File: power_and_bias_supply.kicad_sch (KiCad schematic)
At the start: 42 parts, among them Q501 2N7002, U501 MCP6L02x-xSN, U502 LM2733YMFX/NOPB, U503 TPS22944DCKR, X5 Conn_Coaxial

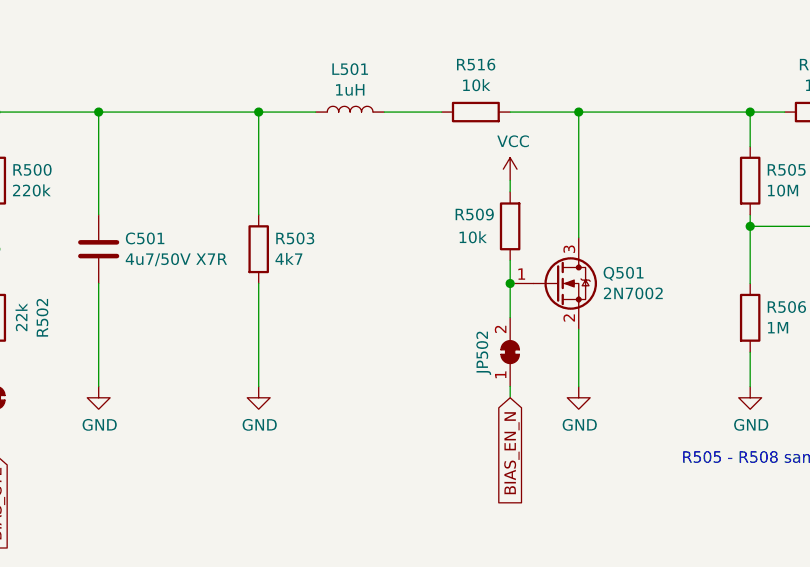
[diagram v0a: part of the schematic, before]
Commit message: Redesign of Board. Added optional Breakoutboars for ADC and DAC
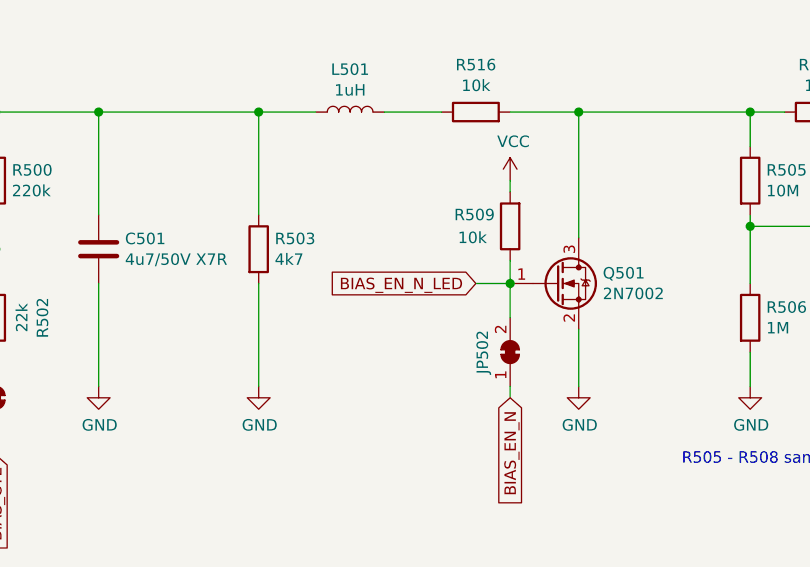
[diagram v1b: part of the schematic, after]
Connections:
- net BIAS_EN_N_LED: now reaches JP502.2 (B), Q501.1 (G), R509.1
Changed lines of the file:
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@@
+    (stroke (width 0) (type solid) (color 0 0 0 0))
+  )
+  (wire (pts (xy 143.51 91.44) (xy 147.32 91.44))
     (stroke (width 0) (type solid) (color 0 0 0 0))
   )
@@
     )
   )
+  (global_label "BIAS_EN_N_LED" (shape input) (at 143.51 91.44 180) (fields_autoplaced)
+    (effects (font (size 1.27 1.27)) (justify right))
+    (property "Intersheet References" "${INTERSHEET_REFS}" (id 0) (at 126.764 91.3606 0)
+      (effects (font (size 1.27 1.27)) (justify right) hide)
+    )
+  )

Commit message: some changes after first test of boards. Package of SN74LV221AD changed to SOIC-16.
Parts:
- C501, C550, C560: JLCplace (none) -> C29823; Supplier (none) -> LCSC
- C503, C504: JLCplace (none) -> C46653; Supplier (none) -> LCSC
- C505: JLCplace (none) -> C1716; Supplier (none) -> LCSC
- C520: JLCplace (none) -> C1710; Supplier (none) -> LCSC
- C553, C554, C569: JLCplace (none) -> C49678; Supplier (none) -> LCSC
- C568: JLCplace (none) -> C28323; Supplier (none) -> LCSC
- D500: Supplier (none) -> LCSC
- JP500, JP501, JP502, JP503, JP504, JP505, JP506, TP502, TP503, TP504, TP505: Supplier (none) -> --
- L500: Supplier LCSC -> Mouser
- Q501: JLCplace (none) -> C8545
- R500: JLCplace (none) -> C17556; Supplier (none) -> LCSC
- R501: JLCplace (none) -> C17455; Supplier (none) -> LCSC
- R502: JLCplace (none) -> C17560; Supplier (none) -> LCSC
- R503: JLCplace (none) -> C17673; Supplier (none) -> LCSC
- R504, R509, R512, R516: JLCplace (none) -> C17414; Supplier (none) -> LCSC
- R505, R507: JLCplace (none) -> C26108; Supplier (none) -> LCSC
- R506, R508: JLCplace (none) -> C17514; Supplier (none) -> LCSC
- U501: JLCBasicPart (none) -> Extended; JLCPartNr (none) -> C623781; JLCType (none) -> MCP6L02T-E/SN
- U503: JLCBasicPart (none) -> Extended; JLCPartNr (none) -> C200357; JLCType (none) -> TPS22944DCKR
- X5: JLCBasicPart (none) -> Extended; JLCPartNr (none) -> C88374; JLCType (none) -> U.FL-R-SMT-1(80); OriginalType (none) -> U.FL-R-SMT-1(80); Supplier (none) -> LCSC

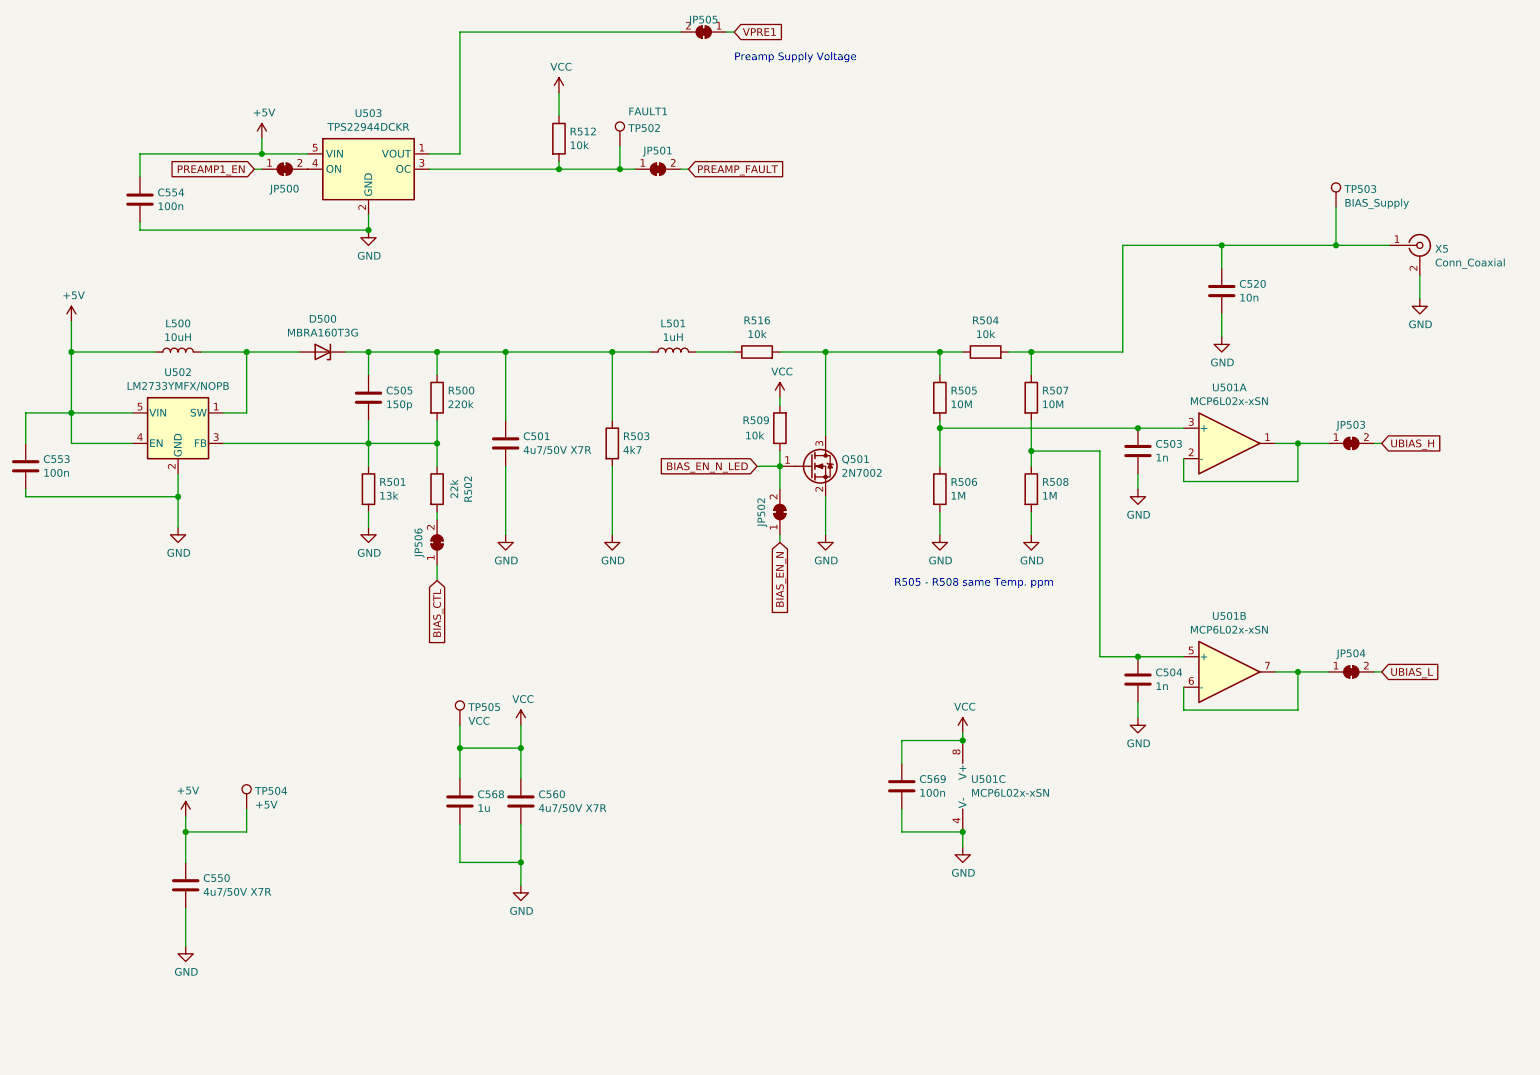
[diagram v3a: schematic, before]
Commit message: Refactored schematic to better show relationship in main schematic
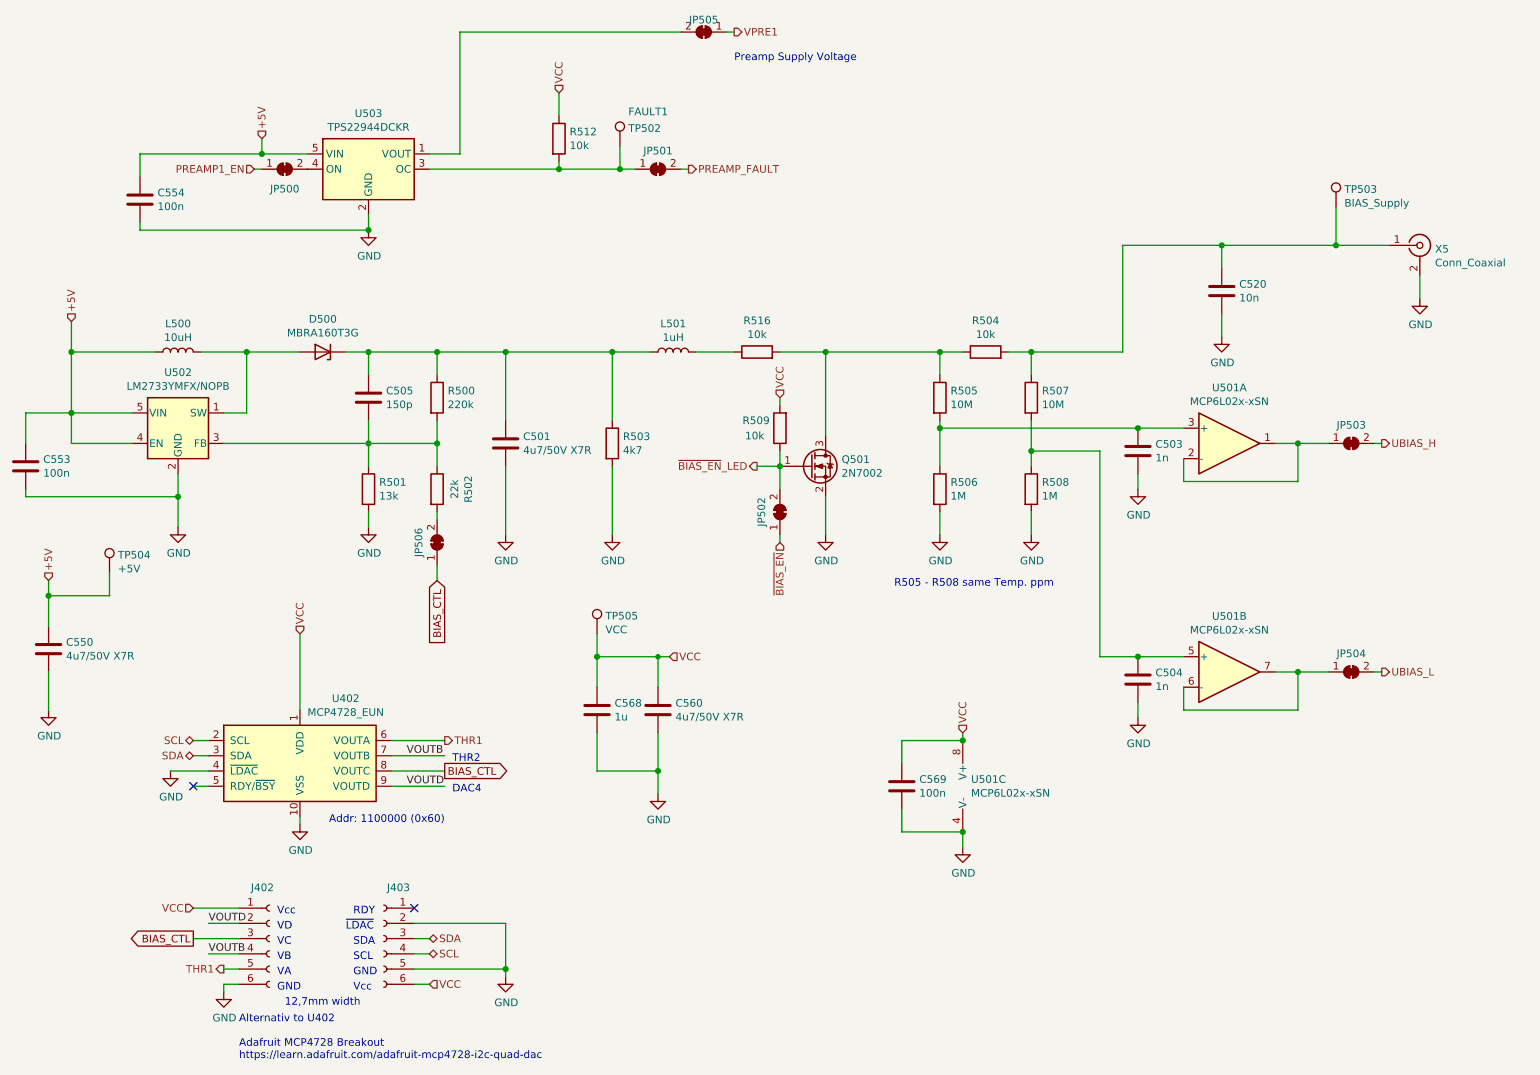
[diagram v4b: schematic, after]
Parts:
- added J402, J403: Conn_01x06_Female, Connector_PinSocket_2.54mm:PinSocket_1x06_P2.54mm_Vertical, symbol Connector:Conn_01x06_Female
- added U402: MCP4728_EUN, Package_SO:MSOP-10_3x3mm_P0.5mm, symbol Analog_DAC:MCP4728
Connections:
- net BIAS_CTL: now also J402.3 (Pin_3), U402.8 (VOUTC)
- net GND: now also J402.6 (Pin_6), J403.2 (Pin_2), J403.5 (Pin_5), U402.10 (VSS), U402.4 (~{LDAC})
- net VCC: now also J402.1 (Pin_1), J403.6 (Pin_6), U402.1 (VDD)
- net BIAS_EN_N renamed ~{BIAS_EN}
- net BIAS_EN_N_LED renamed ~{BIAS_EN}_LED
- new net SCL: J403.4 (Pin_4), U402.2 (SCL)
- new net SDA: J403.3 (Pin_3), U402.3 (SDA)
- new net THR1: J402.5 (Pin_5), U402.6 (VOUTA)
- new net VOUTB: J402.4 (Pin_4), U402.7 (VOUTB)
- new net VOUTD: J402.2 (Pin_2), U402.9 (VOUTD)
- no-connect marks 0 -> 2
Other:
- note added: "12,7mm width"
- note added: "Addr: 1100000 (0x60)"
- note added: "Alternativ to U402 Adafruit MCP4728 Breakout https://learn.adafruit.com/adafruit-mcp4728-i2c-quad-dac"
- note added: "DAC4"
- note added: "GND"
- note added: "RDY"
- note added: "SCL"
- note added: "SDA"
- note added: "THR2"
- note added: "VA"
- note added: "VB"
- note added: "VC"
- note added: "VD"
- note added: "Vcc"
- note added: "~{LDAC}"
- moved on the sheet: C550, C560, C568, TP504, TP505

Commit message: Cleaned up board, replaced GPIO footprint with unshrouded version
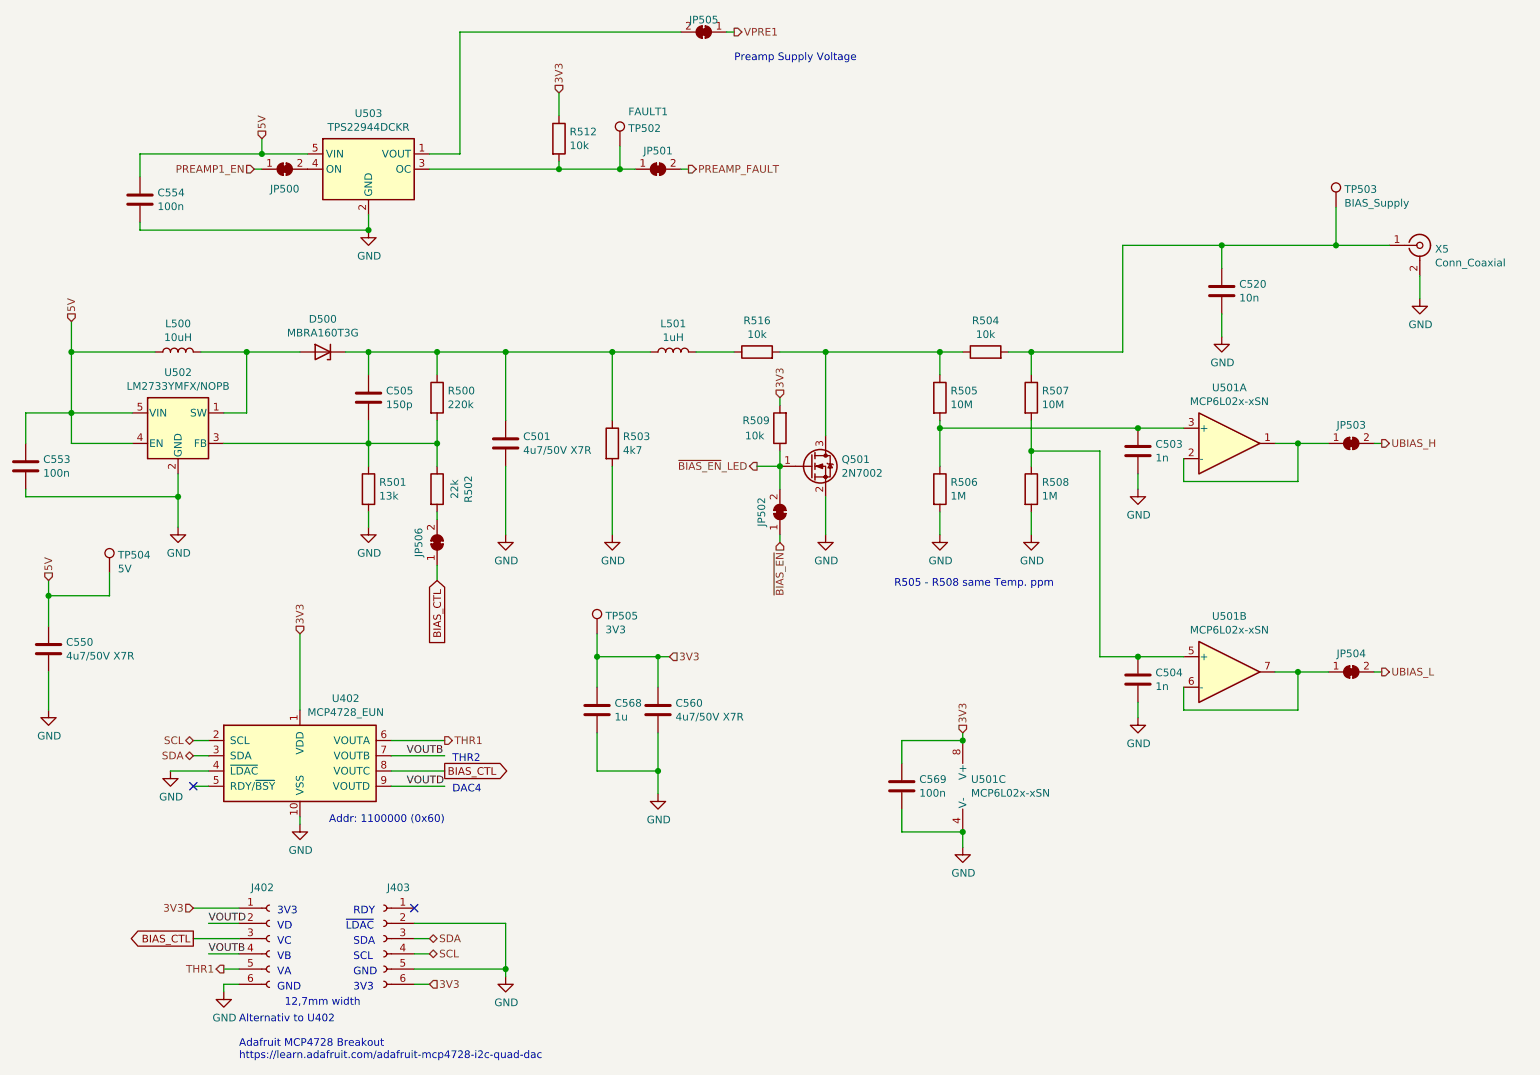
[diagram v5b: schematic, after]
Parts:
- TP504: value +5V -> 5V
- TP505: value VCC -> 3V3
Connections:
- net +5V renamed 5V
- net VCC renamed 3V3
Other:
- note added: "3V3"
- note removed: "Vcc"
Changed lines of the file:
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@@
     (effects (font (size 1.27 1.27)) (justify left bottom))
   )
-  (text "Vcc" (at 63.5 166.37 0)
+  (text "3V3" (at 63.5 166.37 0)
     (effects (font (size 1.27 1.27)) (justify left bottom))
   )
@@
     (effects (font (size 1.27 1.27)) (justify left bottom))
   )
-  (text "Vcc" (at 76.2 179.07 0)
+  (text "3V3" (at 76.2 179.07 0)
     (effects (font (size 1.27 1.27)) (justify left bottom))
   )
@@
     )
   )
-  (hierarchical_label "+5V" (shape input) (at 25.4 110.49 90)
+  (hierarchical_label "5V" (shape input) (at 25.4 110.49 90)
     (effects (font (size 1.27 1.27)) (justify left))
   )
-  (hierarchical_label "+5V" (shape input) (at 29.21 67.31 90)
+  (hierarchical_label "5V" (shape input) (at 29.21 67.31 90)
     (effects (font (size 1.27 1.27)) (justify left))
   )
@@
     (effects (font (size 1.27 1.27)) (justify right))
   )
-  (hierarchical_label "VCC" (shape input) (at 49.53 165.1 180)
+  (hierarchical_label "3V3" (shape input) (at 49.53 165.1 180)
     (effects (font (size 1.27 1.27)) (justify right))
   )
@@
     (effects (font (size 1.27 1.27)) (justify right))
   )
-  (hierarchical_label "+5V" (shape input) (at 60.96 36.83 90)
+  (hierarchical_label "5V" (shape input) (at 60.96 36.83 90)
     (effects (font (size 1.27 1.27)) (justify left))
   )
-  (hierarchical_label "VCC" (shape input) (at 67.31 119.38 90)
+  (hierarchical_label "3V3" (shape input) (at 67.31 119.38 90)
     (effects (font (size 1.27 1.27)) (justify left))
   )
@@
     (effects (font (size 1.27 1.27)) (justify left))
   )
-  (hierarchical_label "VCC" (shape input) (at 88.9 177.8 0)
+  (hierarchical_label "3V3" (shape input) (at 88.9 177.8 0)
     (effects (font (size 1.27 1.27)) (justify left))
   )
@@
     (effects (font (size 1.27 1.27)) (justify left))
   )
-  (hierarchical_label "VCC" (shape input) (at 110.49 29.21 90)
+  (hierarchical_label "3V3" (shape input) (at 110.49 29.21 90)
     (effects (font (size 1.27 1.27)) (justify left))
   )
-  (hierarchical_label "VCC" (shape input) (at 128.905 123.19 0)
+  (hierarchical_label "3V3" (shape input) (at 128.905 123.19 0)
     (effects (font (size 1.27 1.27)) (justify left))
   )
@@
     (effects (font (size 1.27 1.27)) (justify right))
   )
-  (hierarchical_label "VCC" (shape input) (at 147.32 80.01 90)
+  (hierarchical_label "3V3" (shape input) (at 147.32 80.01 90)
     (effects (font (size 1.27 1.27)) (justify left))
   )
@@
     (effects (font (size 1.27 1.27)) (justify right))
   )
-  (hierarchical_label "VCC" (shape input) (at 177.8 135.89 90)
+  (hierarchical_label "3V3" (shape input) (at 177.8 135.89 90)
     (effects (font (size 1.27 1.27)) (justify left))
   )
@@
       (effects (font (size 1.27 1.27)) (justify left))
     )
-    (property "Value" "+5V" (id 1) (at 36.9571 108.5278 0)
+    (property "Value" "5V" (id 1) (at 36.9571 108.5278 0)
       (effects (font (size 1.27 1.27)) (justify left))
     )
@@
       (effects (font (size 1.27 1.27)) (justify left))
     )
-    (property "Value" "VCC" (id 1) (at 118.2371 118.6878 0)
+    (property "Value" "3V3" (id 1) (at 118.2371 118.6878 0)
       (effects (font (size 1.27 1.27)) (justify left))
     )

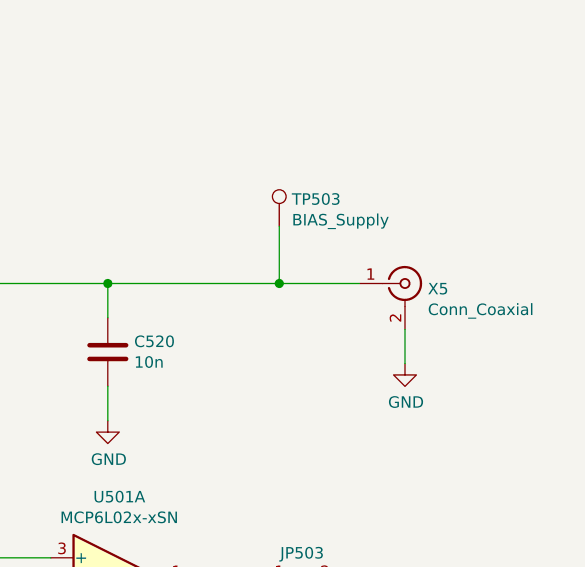
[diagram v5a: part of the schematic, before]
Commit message: Fixed references to library lost in transaction
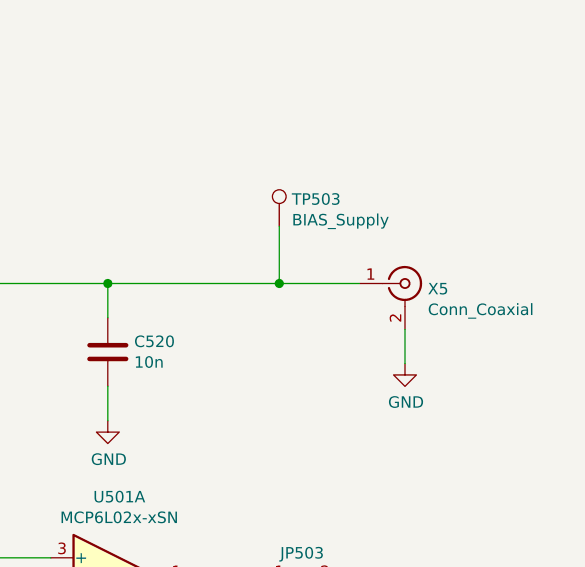
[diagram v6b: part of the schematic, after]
